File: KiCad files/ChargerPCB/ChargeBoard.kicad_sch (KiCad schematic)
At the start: 135 parts, among them IC1 BQ25792RQMR, IC2 TPS25750DRJKR, J1 HRO_TYPE-C-31-M-12, J10 3S/1.5MHz/1A ICGH, J11 4S/1.5MHz/1A ICGH, J2 Conn_01x02, J3 Aardvark, J4 SYS/GND, J5 BAT/GND, J6 Aardvark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

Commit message: renamed some stuff
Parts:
- removed BAT1, BAT2, BAT3, J2: Conn_01x02, Connector_Wire:SolderWire-2sqmm_1x02_P7.8mm_D2mm_OD3.9mm, symbol Connector_Generic:Conn_01x02
- removed C1, C10, C2, C3, C6, C7, C8, C9: 0.1uF 0402, Capacitor_SMD:C_0402_1005Metric, symbol Device:C_Small
- removed C11: 2.2uF 0402, Capacitor_SMD:C_0402_1005Metric, symbol Device:C_Small
- removed Q1, Q2, Q3: BSP89, Package_TO_SOT_SMD:SOT-223-3_TabPin2, symbol Transistor_FET:BSP89
- removed Q4, Q5: AO3401A, Package_TO_SOT_SMD:SOT-23, symbol Transistor_FET:AO3401A
- removed R1, R4, R6: 47 2512, Resistor_SMD:R_2512_6332Metric, symbol Device:R_Small
- removed R103: 51r 2512, Resistor_SMD:R_2512_6332Metric, symbol Device:R_Small
- removed R18, R19, R20, R25, R26, R27: 1K 0402, Resistor_SMD:R_0402_1005Metric, symbol Device:R_Small
- removed R2, R3, R5: 100 0805, Resistor_SMD:R_0805_2012Metric, symbol Device:R_Small
- removed R21, R22: 5.1K 0402, Resistor_SMD:R_0402_1005Metric, symbol Device:R_Small
- removed R23: 1M 0402, Resistor_SMD:R_0402_1005Metric, symbol Device:R_Small
- removed R24: 0r 2512, Resistor_SMD:R_2512_6332Metric, symbol Device:R_Small
- removed U1, U2, U3: HY2213, Package_TO_SOT_SMD:SOT-23-6, symbol HY2213:HY2213
- removed U9: 8254, Package_SO:HTSSOP-16-1EP_4.4x5mm_P0.65mm_EP3.4x5mm, symbol 8254A:8254
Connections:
- net TS: no longer J7.1 (Pin_1), J8.1 (Pin_1), R33.1, R34.2
- new net: J7.1 (Pin_1), J8.1 (Pin_1), R33.1, R34.2
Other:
- note removed: "RCTL"
- note removed: "RSENSE"
- note removed: "RVSS"

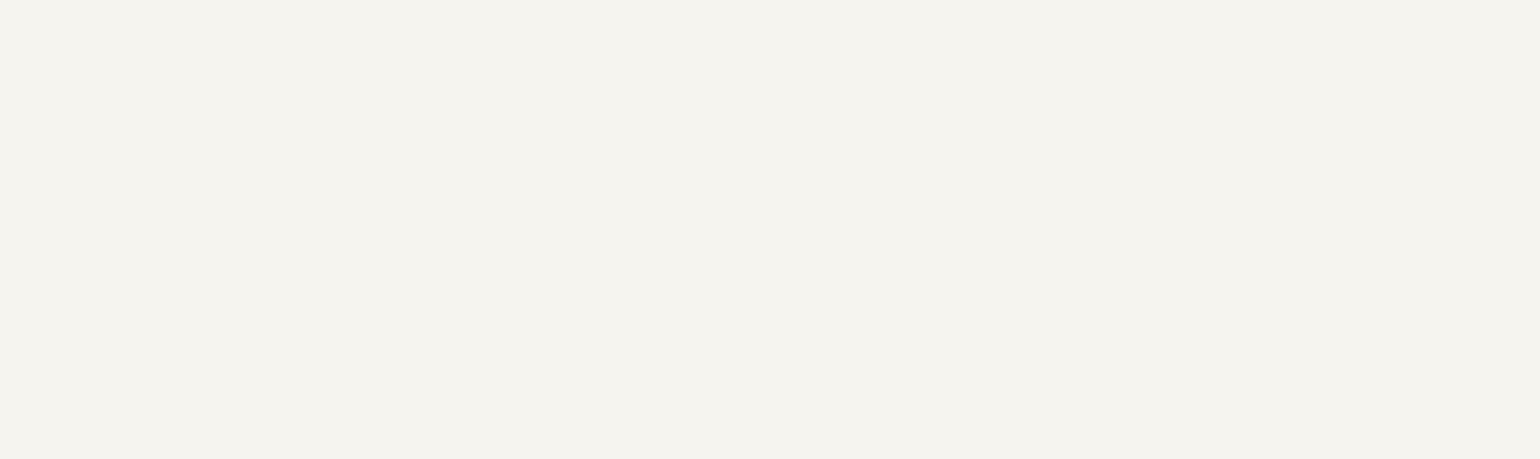
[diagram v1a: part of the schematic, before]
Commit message: added some notes on which 240W capable ICs to switch to.
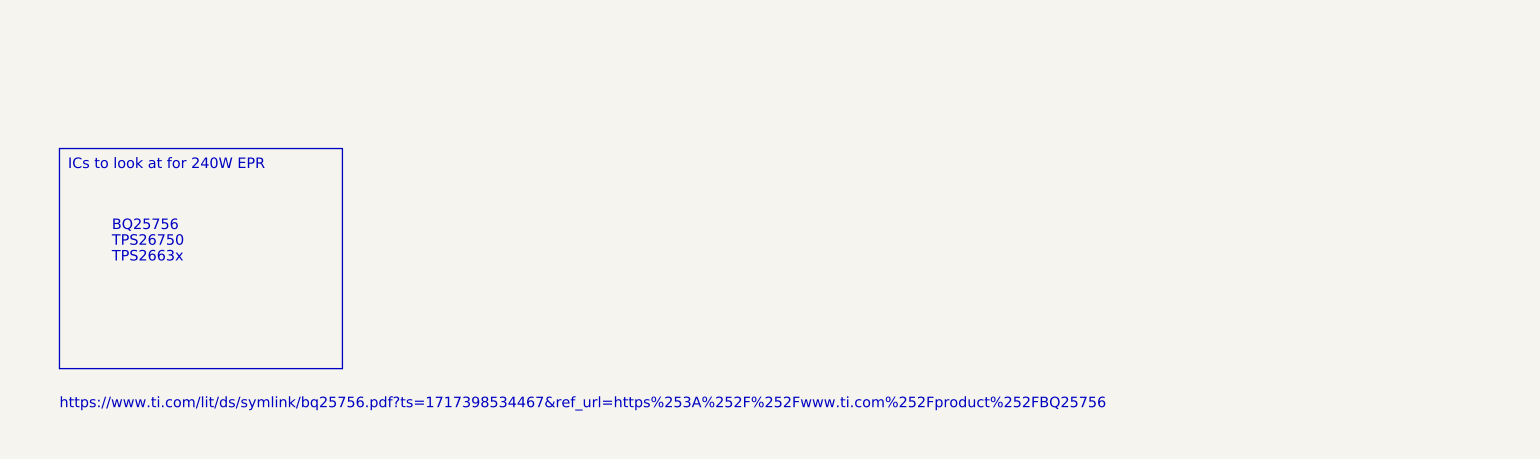
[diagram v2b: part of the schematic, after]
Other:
- note added: "BQ25756"
- note added: "TPS2663x"
- note added: "TPS26750"
- note added: "https://www.ti.com/lit/ds/symlink/bq25756.pdf?ts=1717398534467&ref_url=https%253A%252F%252Fwww.ti.com%252Fproduct%252FBQ25756"
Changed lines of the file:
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@@
     (stroke (width 0) (type default))
+  )
+  (text_box "ICs to look at for 240W EPR"
+    (at 20.32 180.975 0) (size 34.29 26.67)
+    (stroke (width 0) (type default))
+    (fill (type none))
+    (effects (font (size 1.27 1.27)) (justify left top))
+  )
+  (text "TPS26750" (at 26.67 193.04 0)
+    (effects (font (size 1.27 1.27)) (justify left bottom))
+  )
+  (text "TPS2663x" (at 26.67 194.945 0)
+    (effects (font (size 1.27 1.27)) (justify left bottom))
+  )
+  (text "BQ25756" (at 26.67 191.135 0)
+    (effects (font (size 1.27 1.27)) (justify left bottom))
   )
   (text "Need to swap for BQ25731\neventually" (at 287.02 92.71 0)
     (effects (font (size 1.27 1.27) (thickness 0.254) bold) (justify left bottom))
   )
+  (text "https://www.ti.com/lit/ds/symlink/bq25756.pdf?ts=1717398534467&ref_url=https%253A%252F%252Fwww.ti.com%252Fproduct%252FBQ25756"
+    (at 20.32 212.725 0)
+    (effects (font (size 1.27 1.27)) (justify left bottom) (href "https://www.ti.com/lit/ds/symlink/bq25756.pdf?ts=1717398534467&ref_url=https%253A%252F%252Fwww.ti.com%252Fproduct%252FBQ25756"))
+  )
   (global_label "BTST2" (shape input) (at 318.135 106.68 0) (fields_autoplaced)
